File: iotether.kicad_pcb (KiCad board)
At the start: 2 copper layers, 92 x 100 mm, 179 parts, among them J1 Conn_02x03_Counter_Clockwise, J101 USB_B_Micro, J102 Barrel_Jack, J103 Conn_02x04_Odd_Even, J201 Conn_02x04_Top_Bottom, J202 8P8C_LED_Shielded, J205 Conn_01x04, J206 Conn_01x04, J207 Conn_01x04, J208 Conn_01x04, J301 Conn_01x12, J302 Conn_01x12, J303 Conn_01x12, J304 Conn_01x12, J305 Conn_02x04_Odd_Even, J306 Conn_01x09, J307 Conn_01x09, J308 Conn_02x04_Odd_Even, SW1 SW_SPDT, SW301 SW_Push, SW302 SW_Push, SW303 SW_Push, SW304 SW_Push, U101 LAN9514, U102 93CxxC, U103 LM1117-3.3, U104 MCP73831-2-OT, U105 AP62200, U201 SN74CBT3253, U301 FT4232H, U302 93CxxC, U303 ATmega328P-P, U304 FE1.1s, U408 LM75B, U409 DS1307+, Y101 Crystal, Y301 Crystal, Y302 Crystal, Y303 Crystal, Y401 Crystal

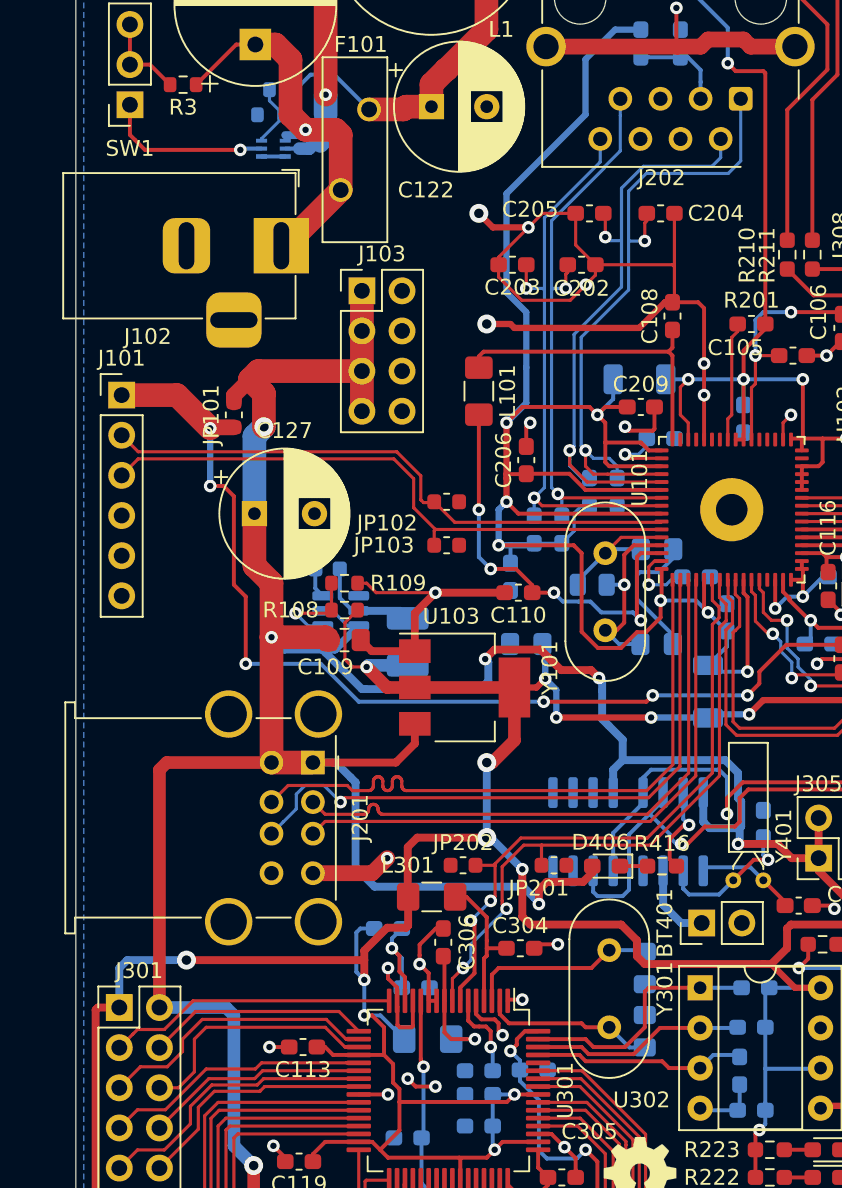
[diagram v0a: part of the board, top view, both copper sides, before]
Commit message: IoTether: Add USB-C
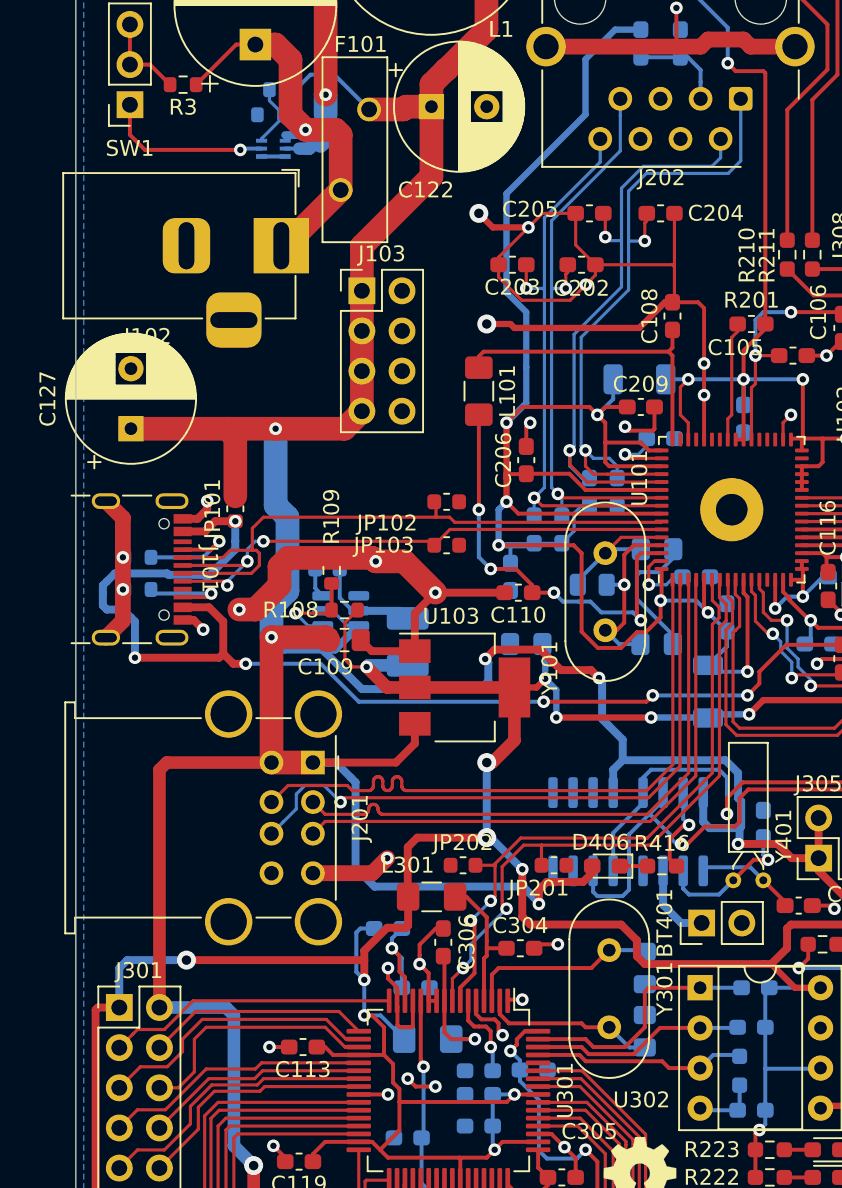
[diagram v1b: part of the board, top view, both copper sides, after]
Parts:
- added R110: R, Resistor_SMD:R_0603_1608Metric, B.Cu at (78.9, 96.3)
- added R111: R, Resistor_SMD:R_0603_1608Metric, B.Cu at (78.9, 98.3)
- J101: value USB_B_Micro -> USB_C_Receptacle_USB2.0; footprint Connector_PinHeader_2.54mm:PinHeader_1x06_P2.54mm_Vertical -> Library:USB_C_Receptacle_GCT_USB4105-xx-A_16P_TopMnt_Horizontal
- R304: footprint Resistor_SMD:R_0603_1608Metric_Pad1.05x0.95mm_HandSolder -> Resistor_SMD:R_0603_1608Metric_Pad0.98x0.95mm_HandSolder
- moved J101 11.0 mm to (78.0, 97.0), turned to -90 degrees
- moved C127 9.48 mm to (78.5, 88.1), turned to 90 degrees
- moved JP101 5.94 mm to (85.1, 93.2)
- moved R109 1.15 mm to (91.2, 97.1), turned to 90 degrees
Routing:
- net GND: track 223.0 -> 246.6 mm, vias 39 -> 45
- net +5V: track 600.7 -> 621.1 mm
- net VBUS: track 65.0 -> 74.0 mm
- net Net-(J101-PadA5): track 0.00 -> 7.27 mm, vias 0 -> 1
- net Net-(J101-PadB5): track 0.00 -> 5.82 mm, vias 0 -> 1
- net UP_D-: track 37.4 -> 39.8 mm
- net UP_D+: track 38.5 -> 36.9 mm, vias 0 -> 3

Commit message: iotether
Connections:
- U105 pad 5: +5V -> unconnected-(U105-Pad5)
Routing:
- net +5V: track 621.1 -> 618.5 mm
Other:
- board text added: "IoTether Rev. 5 2025-03-16 website.peterjin.org/wiki/IoTether"
- board text removed: "IoTether Rev. 4 2024-03-10 website.peterjin.org/wiki/IoTether"
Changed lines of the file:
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@@
       (drillshape 0)
       (scaleselection 1)
-      (outputdirectory "/home/daniel/gitprojects-1/gerbers2")
+      (outputdirectory "/home/sebastian/Documents/gerbers/")
     )
   )
@@
   (net 182 "Net-(J101-PadB5)")
   (net 183 "unconnected-(J101-PadB8)")
+  (net 184 "unconnected-(U105-Pad5)")
   (footprint "Capacitor_SMD:C_0603_1608Metric_Pad1.05x0.95mm_HandSolder" (layer "F.Cu")
     (at 120.375 83.5)
@@
       (net 176 "Net-(R108-Pad2)") (pinfunction "Pin_4") (pintype "passive"))
     (pad "5" smd roundrect (at 1.1375 0 180) (size 1.325 0.6) (layers "B.Cu" "B.Paste" "B.Mask") (roundrect_rratio 0.25)
-      (net 6 "+5V") (pinfunction "Pin_5") (pintype "passive"))
+      (net 184 "unconnected-(U105-Pad5)") (pinfunction "Pin_5") (pintype "passive"))
     (pad "6" smd roundrect (at 1.1375 0.95 180) (size 1.325 0.6) (layers "B.Cu" "B.Paste" "B.Mask") (roundrect_rratio 0.25)
       (net 175 "Net-(C126-Pad2)") (pinfunction "Pin_6") (pintype "passive"))
@@
   (gr_line (start 167 50) (end 167 150) (layer "Edge.Cuts") (width 0.05))
   (gr_line (start 167 150) (end 75 150) (layer "Edge.Cuts") (width 0.05))
-  (gr_text "IoTether Rev. 4 2024-03-10\nwebsite.peterjin.org/wiki/IoTether" (at 103 140.75) (layer "F.SilkS")
+  (gr_text "IoTether Rev. 5 2025-03-16\nwebsite.peterjin.org/wiki/IoTether" (at 103 140.75) (layer "F.SilkS")
     (effects (font (size 1 1) (thickness 0.25)))
   )
@@
   (segment (start 100.6 104.6) (end 101.1 104.1) (width 0.5) (layer "B.Cu") (net 6))
   (segment (start 135.725 66.6) (end 135.7 66.625) (width 1.5) (layer "B.Cu") (net 6))
-  (segment (start 91.25 99.65) (end 92.2 100.6) (width 0.2) (layer "B.Cu") (net 6))
   (segment (start 89.05 144.46) (end 89.05 140.8) (width 0.8) (layer "B.Cu") (net 6))
   (segment (start 89.8525 65.7225) (end 91.355 65.7225) (width 0.25) (layer "B.Cu") (net 6))
@@
   (segment (start 88.2 102.1) (end 87.4 101.3) (width 0.5) (layer "B.Cu") (net 6))
   (segment (start 90.6 102.1) (end 88.2 102.1) (width 0.5) (layer "B.Cu") (net 6))
-  (segment (start 92.2 100.6) (end 92.9 100.6) (width 0.2) (layer "B.Cu") (net 6))
-  (segment (start 90.625 99.65) (end 91.25 99.65) (width 0.2) (layer "B.Cu") (net 6))
   (segment (start 145.1 64.8) (end 145.5 65.2) (width 1.5) (layer "B.Cu") (net 6))
   (segment (start 103.8 51.6) (end 127.3 51.6) (width 1.5) (layer "B.Cu") (net 6))
